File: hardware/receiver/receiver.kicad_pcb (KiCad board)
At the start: 2 copper layers, 36 x 73.5 mm, 3 parts, among them J1 Conn_01x07_Socket, J2 Conn_01x02_Socket, U1 Pico

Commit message: Update receiver PCB
Power and ground planes added
Logo and title added to silkscreen
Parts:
- added G***: LOGO, LOGO, F.Cu at (122.5, 70.5)
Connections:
- U1 pad 3: unconnected-(U1-GND-Pad3) -> /GND
- U1 pad 38: unconnected-(U1-GND-Pad38) -> /GND
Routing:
- net /GND: track 82.7 -> 0.98 mm
- net /3V3: track 54.3 -> 0.00 mm
- added copper zone on B.Cu, net /3V3
- added copper zone on F.Cu, net /GND
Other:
- board text added: "Low-Cost Thrust Stand Sensing Receiver Rev 1.0"

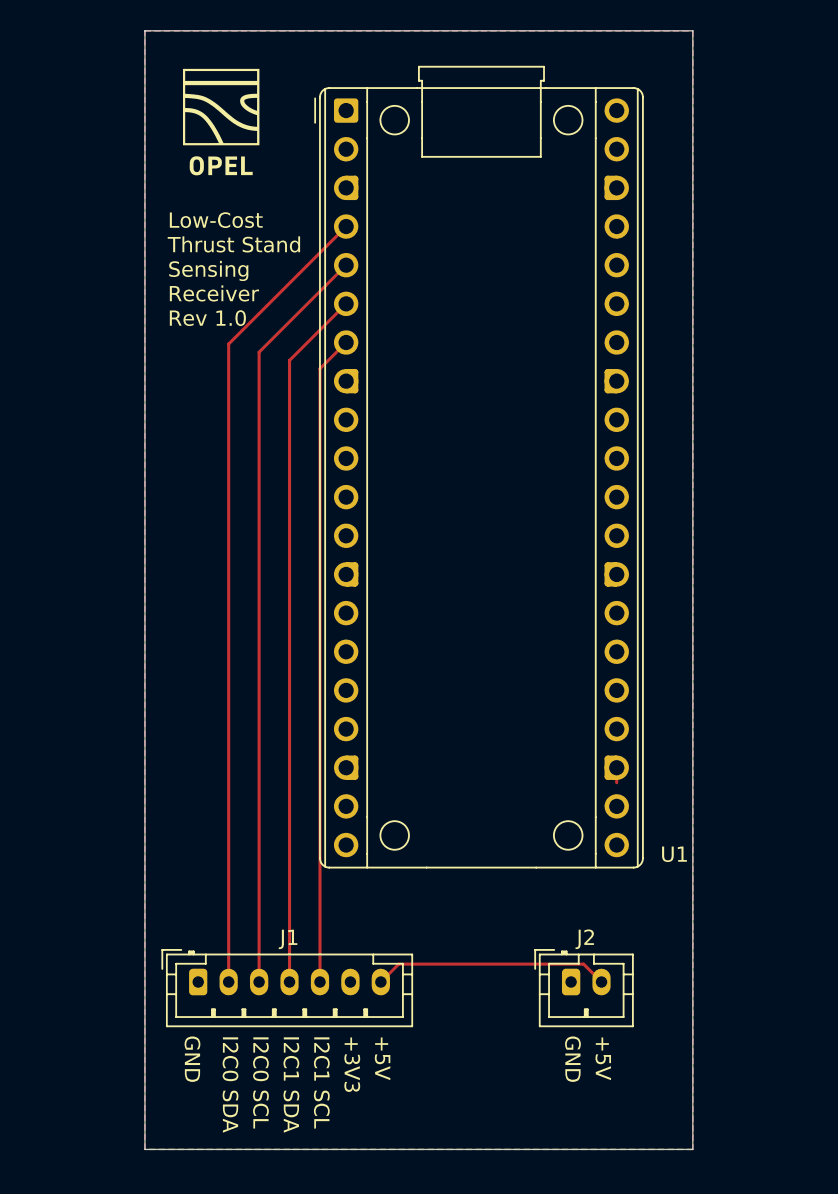
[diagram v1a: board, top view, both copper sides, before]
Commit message: Update receiver PCB and add gerber files
Added mounting holes, changes silk screen, and organized the schematic
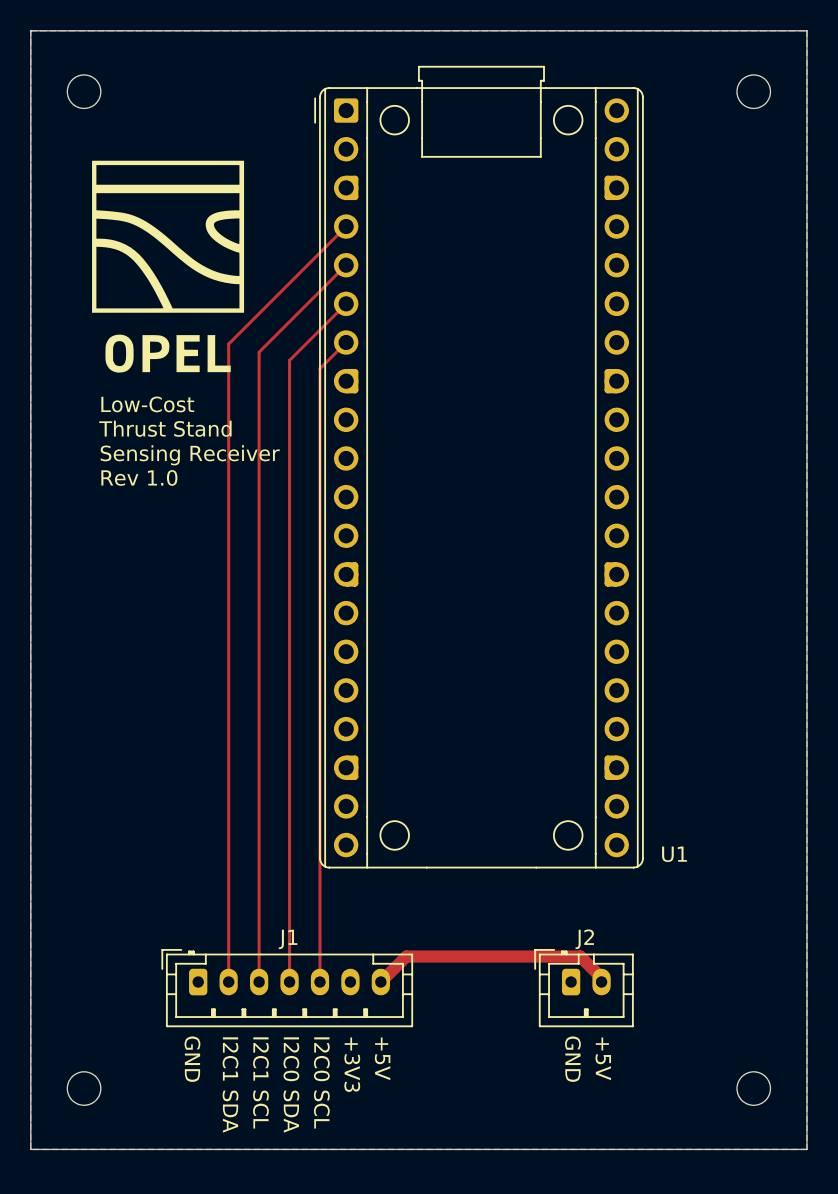
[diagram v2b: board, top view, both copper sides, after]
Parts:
- added H1: MountingHole, MountingHole:MountingHole_2.2mm_M2, F.Cu at (113.5, 68.5)
- added H2: MountingHole, MountingHole:MountingHole_2.2mm_M2, F.Cu at (157.5, 68.5)
- added H3: MountingHole, MountingHole:MountingHole_2.2mm_M2, F.Cu at (113.5, 134.0)
- added H4: MountingHole, MountingHole:MountingHole_2.2mm_M2, F.Cu at (157.5, 134.0)
- moved G*** 10.1 mm to (119.0, 80.0)
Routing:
- net /GND: track 0.98 -> 0.00 mm
- net /+5V: track 15.5 -> 16.0 mm
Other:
- board size 36 x 73.5 mm -> 51 x 73.5 mm

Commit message: Rename Sensing_PCB to sender
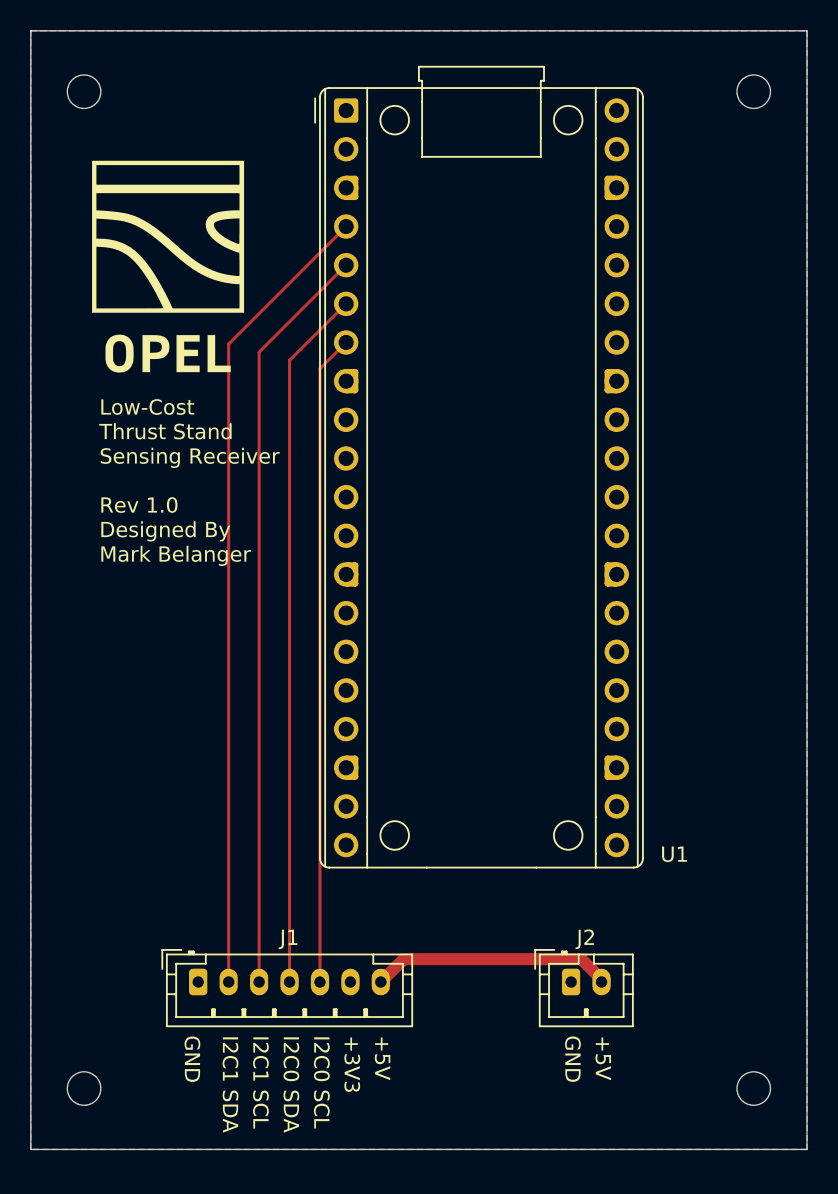
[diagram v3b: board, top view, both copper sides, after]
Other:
- board text added: "Low-Cost Thrust Stand Sensing Receiver Rev 1.0 Designed By Mark Belanger"
- board text removed: "Low-Cost Thrust Stand Sensing Receiver Rev 1.0"
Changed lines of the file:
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@@
 		)
 	)
-	(gr_text "Low-Cost\nThrust Stand\nSensing Receiver\nRev 1.0"
-		(at 114.5 94.5 0)
+	(gr_text "Low-Cost\nThrust Stand\nSensing Receiver\n\nRev 1.0\nDesigned By\nMark Belanger"
+		(at 114.5 99.5 0)
 		(layer "F.SilkS")
 		(effects
@@
 	)
 	(segment
-		(start 133 127)
-		(end 134.675 125.325)
-		(width 0.8)
-		(layer "F.Cu")
-		(net 5)
-	)
-	(segment
-		(start 146.1 125.325)
-		(end 147.5 126.725)
-		(width 0.8)
-		(layer "F.Cu")
-		(net 5)
-	)
-	(segment
 		(start 147.5 126.725)
 		(end 147.5 127)
@@
 	)
 	(segment
-		(start 134.675 125.325)
-		(end 146.1 125.325)
+		(start 147.5 126.81599)
+		(end 146.18401 125.5)
 		(width 0.8)
 		(layer "F.Cu")
+		(net 5)
+	)
+	(segment
+		(start 147.5 127)
+		(end 147.5 126.81599)
+		(width 0.8)
+		(layer "F.Cu")
+		(net 5)
+	)
+	(segment
+		(start 134.5 125.5)
+		(end 133 127)
+		(width 0.8)
+		(layer "F.Cu")
+		(net 5)
+	)
+	(segment
+		(start 146.18401 125.5)
+		(end 134.5 125.5)
+		(width 0.8)
+		(layer "F.Cu")
